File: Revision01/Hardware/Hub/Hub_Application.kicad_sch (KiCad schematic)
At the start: 81 parts, among them J10 IDC 6Pin Male Header, J11 IDC 6Pin Male Header, J12 IDC 6Pin Male Header, J13 IDC 6Pin Male Header, J14 IDC 6Pin Male Header, J15 IDC 6Pin Female Socket, J16 IDC 6Pin Male Header, J17 IDC 6Pin Female Socket, J18 IDC 6Pin Female Socket, J19 SMA-J-P-H-ST-EM1, J6 IDC 6Pin Male Header, J7 IDC 6Pin Male Header, J8 IDC 6Pin Male Header, J9 IDC 6Pin Male Header, Q1 PMOS, Q2 NMOS, Q3 PMOS, U3 MPU-6500, U4 Adafruit 3070

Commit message: . Moved / Renamed "Revision01" libraries to "Hub"
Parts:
- J10, J11, J12, J13, J14, J16, J6, J7, J8, J9: footprint Revision01:AdamTech_BHR-06-VUA -> Hub:AdamTech_BHR-06-VUA; symbol Revision01:IDC_6Pin_Male_Header -> Hub:IDC_6Pin_Male_Header
- J15, J17, J18: symbol Revision01:IDC_6Pin_Female_Socket -> Hub:IDC_6Pin_Female_Socket
- J19: symbol Revision01:ANT_SMA_Edge -> Hub:ANT_SMA_Edge
- R10: symbol Revision01:StrainGaugeFullBridge -> Hub:StrainGaugeFullBridge
- U3: footprint Revision01:MPU-6500_QFN40P300X300X95-25N -> Hub:MPU-6500_QFN40P300X300X95-25N; symbol Revision01:MPU-6500 -> Hub:MPU-6500
- U4: footprint Revision01:Adafruit3070 -> Hub:Adafruit3070; symbol Revision01:Adafruit3070 -> Hub:Adafruit3070
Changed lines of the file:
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@@
 	)
 	(symbol
-		(lib_id "Revision01:IDC_6Pin_Male_Header")
+		(lib_id "Hub:IDC_6Pin_Male_Header")
 		(at 66.04 195.58 0)
 		(unit 1)
@@
 			)
 		)
-		(property "Footprint" "Revision01:AdamTech_BHR-06-VUA"
+		(property "Footprint" "Hub:AdamTech_BHR-06-VUA"
 			(at 66.04 195.58 0)
 			(effects
@@
 	)
 	(symbol
-		(lib_id "Revision01:IDC_6Pin_Male_Header")
+		(lib_id "Hub:IDC_6Pin_Male_Header")
 		(at 148.59 118.11 0)
 		(unit 1)
@@
 			)
 		)
-		(property "Footprint" "Revision01:AdamTech_BHR-06-VUA"
+		(property "Footprint" "Hub:AdamTech_BHR-06-VUA"
 			(at 148.59 118.11 0)
 			(effects
@@
 	)
 	(symbol
-		(lib_id "Revision01:IDC_6Pin_Male_Header")
+		(lib_id "Hub:IDC_6Pin_Male_Header")
 		(at 148.59 80.01 0)
 		(unit 1)
@@
 			)
 		)
-		(property "Footprint" "Revision01:AdamTech_BHR-06-VUA"
+		(property "Footprint" "Hub:AdamTech_BHR-06-VUA"
 			(at 148.59 80.01 0)
 			(effects
@@
 	)
 	(symbol
-		(lib_id "Revision01:IDC_6Pin_Male_Header")
+		(lib_id "Hub:IDC_6Pin_Male_Header")
 		(at 148.59 105.41 0)
 		(unit 1)
@@
 			)
 		)
-		(property "Footprint" "Revision01:AdamTech_BHR-06-VUA"
+		(property "Footprint" "Hub:AdamTech_BHR-06-VUA"
 			(at 148.59 105.41 0)
 			(effects
@@
 	)
 	(symbol
-		(lib_id "Revision01:ANT_SMA_Edge")
+		(lib_id "Hub:ANT_SMA_Edge")
 		(at 349.25 203.2 0)
 		(unit 1)
@@
 	)
 	(symbol
-		(lib_id "Revision01:Adafruit3070")
+		(lib_id "Hub:Adafruit3070")
 		(at 285.75 179.07 0)
 		(unit 1)
@@
 			)
 		)
-		(property "Footprint" "Revision01:Adafruit3070"
+		(property "Footprint" "Hub:Adafruit3070"
 			(at 285.75 179.07 0)
 			(effects
@@
 	)
 	(symbol
-		(lib_id "Revision01:IDC_6Pin_Male_Header")
+		(lib_id "Hub:IDC_6Pin_Male_Header")
 		(at 148.59 168.91 0)
 		(unit 1)
@@
 			)
 		)
-		(property "Footprint" "Revision01:AdamTech_BHR-06-VUA"
+		(property "Footprint" "Hub:AdamTech_BHR-06-VUA"
 			(at 148.59 168.91 0)
 			(effects
@@
 	)
 	(symbol
-		(lib_id "Revision01:StrainGaugeFullBridge")
+		(lib_id "Hub:StrainGaugeFullBridge")
 		(at 149.86 53.34 0)
 		(unit 1)
@@
 	)
 	(symbol
-		(lib_id "Revision01:IDC_6Pin_Male_Header")
+		(lib_id "Hub:IDC_6Pin_Male_Header")
 		(at 101.6 195.58 0)
 		(unit 1)
@@
 			)
 		)
-		(property "Footprint" "Revision01:AdamTech_BHR-06-VUA"
+		(property "Footprint" "Hub:AdamTech_BHR-06-VUA"
 			(at 101.6 195.58 0)
 			(effects
@@
 	)
 	(symbol
-		(lib_id "Revision01:IDC_6Pin_Female_Socket")
+		(lib_id "Hub:IDC_6Pin_Female_Socket")
 		(at 83.82 195.58 0)
 		(mirror y)
@@
 	)
 	(symbol
-		(lib_id "Revision01:IDC_6Pin_Male_Header")
+		(lib_id "Hub:IDC_6Pin_Male_Header")
 		(at 148.59 143.51 0)
 		(unit 1)
@@
 			)
 		)
-		(property "Footprint" "Revision01:AdamTech_BHR-06-VUA"
+		(property "Footprint" "Hub:AdamTech_BHR-06-VUA"
 			(at 148.59 143.51 0)
 			(effects
@@
 	)
 	(symbol
-		(lib_id "Revision01:MPU-6500")
+		(lib_id "Hub:MPU-6500")
 		(at 321.31 110.49 0)
 		(unit 1)
@@
 			)
 		)
-		(property "Footprint" "Revision01:MPU-6500_QFN40P300X300X95-25N"
+		(property "Footprint" "Hub:MPU-6500_QFN40P300X300X95-25N"
 			(at 321.31 93.98 0)
 			(effects
@@
 	)
 	(symbol
-		(lib_id "Revision01:IDC_6Pin_Female_Socket")
+		(lib_id "Hub:IDC_6Pin_Female_Socket")
 		(at 120.65 195.58 0)
 		(mirror y)
@@
 	)
 	(symbol
-		(lib_id "Revision01:IDC_6Pin_Male_Header")
+		(lib_id "Hub:IDC_6Pin_Male_Header")
 		(at 148.59 92.71 0)
 		(unit 1)
@@
 			)
 		)
-		(property "Footprint" "Revision01:AdamTech_BHR-06-VUA"
+		(property "Footprint" "Hub:AdamTech_BHR-06-VUA"
 			(at 148.59 92.71 0)
 			(effects
@@
 	)
 	(symbol
-		(lib_id "Revision01:IDC_6Pin_Male_Header")
+		(lib_id "Hub:IDC_6Pin_Male_Header")
 		(at 148.59 156.21 0)
 		(unit 1)
@@
 			)
 		)
-		(property "Footprint" "Revision01:AdamTech_BHR-06-VUA"
+		(property "Footprint" "Hub:AdamTech_BHR-06-VUA"
 			(at 148.59 156.21 0)
 			(effects
@@
 	)
 	(symbol
-		(lib_id "Revision01:IDC_6Pin_Female_Socket")
+		(lib_id "Hub:IDC_6Pin_Female_Socket")
 		(at 133.35 195.58 0)
 		(unit 1)
@@
 	)
 	(symbol
-		(lib_id "Revision01:IDC_6Pin_Male_Header")
+		(lib_id "Hub:IDC_6Pin_Male_Header")
 		(at 148.59 130.81 0)
 		(unit 1)
@@
 			)
 		)
-		(property "Footprint" "Revision01:AdamTech_BHR-06-VUA"
+		(property "Footprint" "Hub:AdamTech_BHR-06-VUA"
 			(at 148.59 130.81 0)
 			(effects

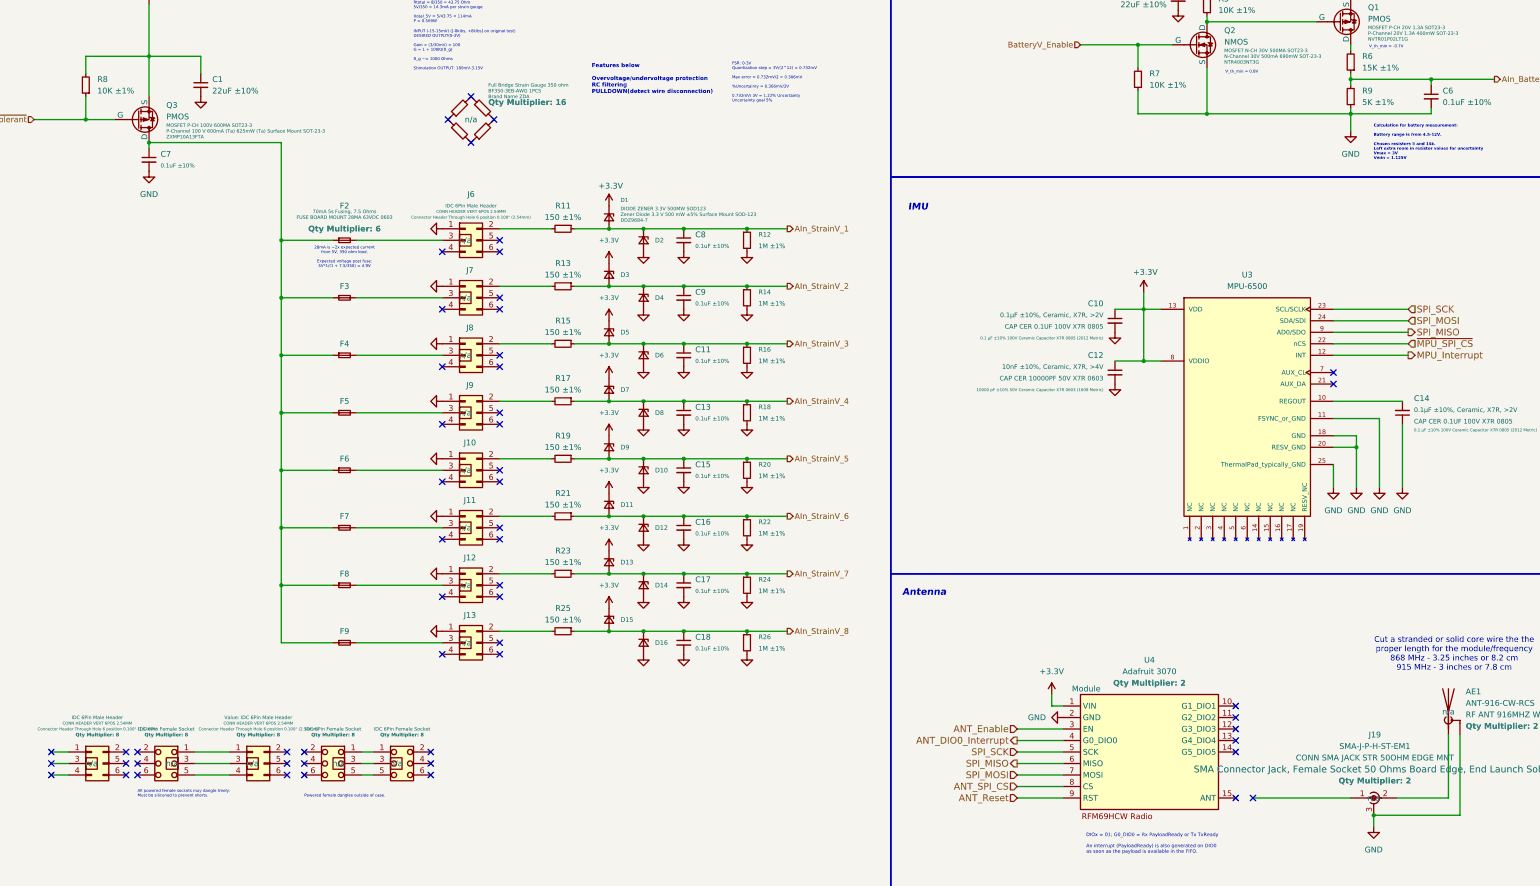
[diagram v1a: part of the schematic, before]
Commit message: . Split Hub symbol fields for Distributor Link/Part into DigiKey & AliExpress Link/Part in preparation for Mouser column.
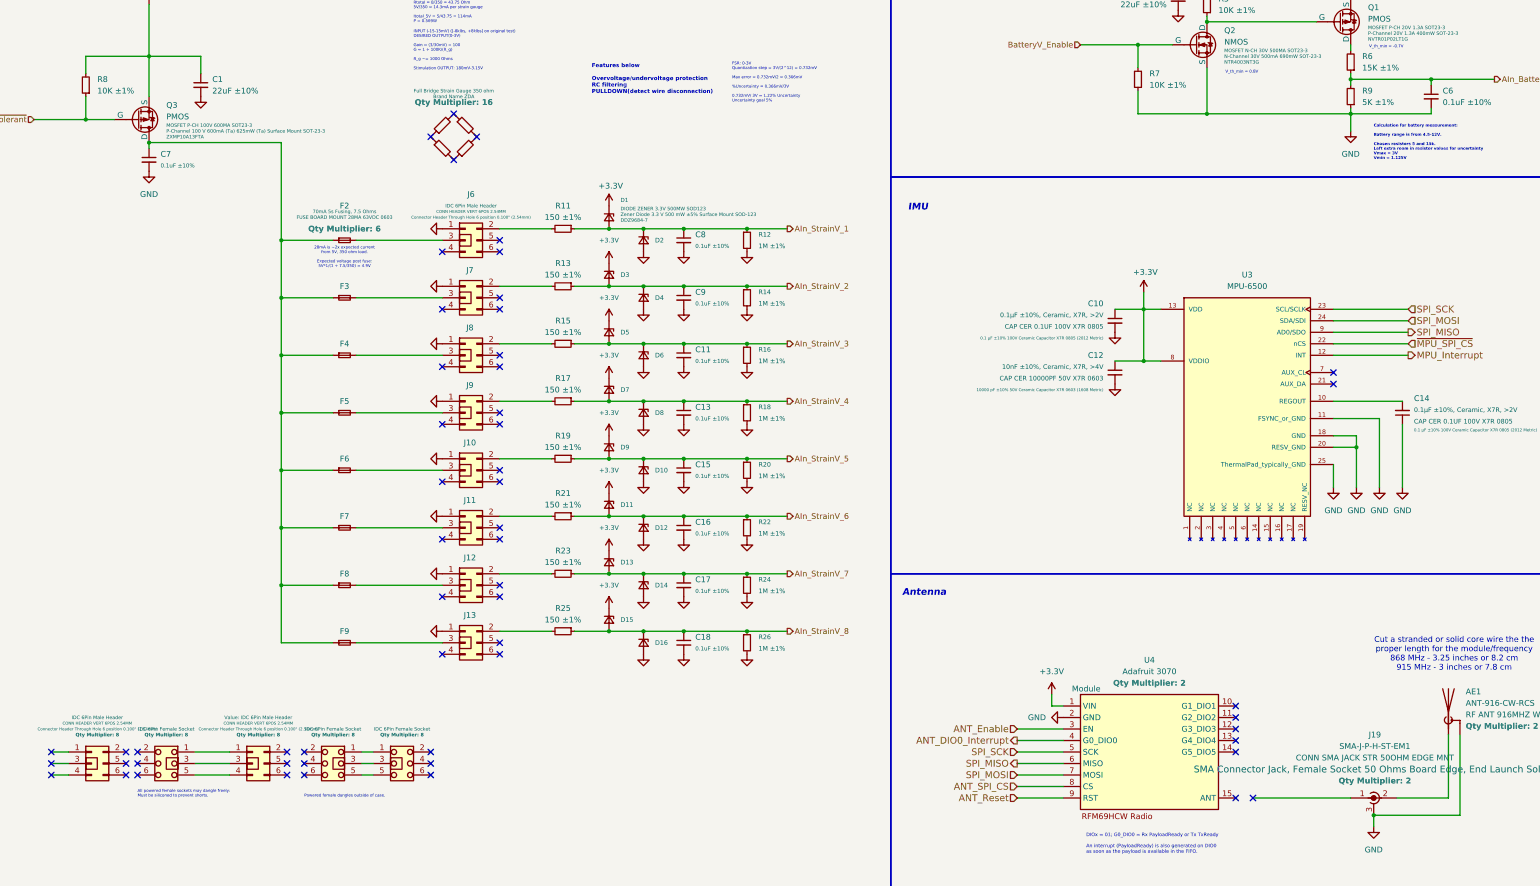
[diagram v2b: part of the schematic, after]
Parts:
- AE1: DigiKey Link (none) -> https://www.digikey.ca/en/products/detail/te-connectivity-l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; DigiKey Part Number (none) -> ANT-916-CW-RCS-ND; Distributor Link https://www.digikey.ca/en/products/detail/te-connectivity-l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 -> (none); Distributor Part Number ANT-916-CW-RCS-ND -> (none)
- C1, C19: DigiKey Link (none) -> https://www.digikey.ca/en/products/detail/samsung-electro-m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; DigiKey Part Number (none) -> 1276-3047-1-ND - Cut Tape (CT); Distributor Link https://www.digikey.ca/en/products/detail/samsung-electro-m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 -> (none); Distributor Part Number 1276-3047-1-ND - Cut Tape (CT) -> (none)
- C10, C11, C13, C14, C15, C16, C17, C18, C6, C7, C8, C9: DigiKey Link (none) -> https://www.digikey.ca/en/products/detail/samsung-electro-m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; DigiKey Part Number (none) -> 1276-6840-1-ND - Cut Tape (CT); Distributor Link https://www.digikey.ca/en/products/detail/samsung-electro-m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 -> (none); Distributor Part Number 1276-6840-1-ND - Cut Tape (CT) -> (none)
- C12: DigiKey Link (none) -> https://www.digikey.ca/en/products/detail/samsung-electro-m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; DigiKey Part Number (none) -> 1276-CL10B103KB8WPNDCT-ND - Cut Tape (CT); Distributor Link https://www.digikey.ca/en/products/detail/samsung-electro-m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 -> (none); Distributor Part Number 1276-CL10B103KB8WPNDCT-ND - Cut Tape (CT) -> (none)
- D1, D10, D11, D12, D13, D14, D15, D16, D2, D3, D4, D5, D6, D7, D8, D9: DigiKey Link (none) -> https://www.digikey.ca/en/products/detail/diodes-incorporat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; DigiKey Part Number (none) -> DDZ9684-7DITR-ND; Distributor Link https://www.digikey.ca/en/products/detail/diodes-incorporat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 -> (none); Distributor Part Number DDZ9684-7DITR-ND -> (none)
- F2, F3, F4, F5, F6, F7, F8, F9: DigiKey Link (none) -> https://www.digikey.ca/en/products/detail/kyocera-avx/F0603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; DigiKey Part Number (none) -> 478-13097-1-ND - Cut Tape (CT); Distributor Link https://www.digikey.ca/en/products/detail/kyocera-avx/F0603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 -> (none); Distributor Part Number 478-13097-1-ND - Cut Tape (CT) -> (none)
- J10, J11, J12, J13, J14, J16, J6, J7, J8, J9: DigiKey Link (none) -> https://www.digikey.ca/en/products/detail/adam-tech/BHR-06-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; DigiKey Part Number (none) -> 2057-BHR-06-VUA-ND; Distributor Link https://www.digikey.ca/en/products/detail/adam-tech/BHR-06-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 -> (none); Distributor Part Number 2057-BHR-06-VUA-ND -> (none)
- J15, J17, J18: DigiKey Link (none) -> https://www.digikey.ca/en/products/detail/adam-tech/FCS-06-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; DigiKey Part Number (none) -> 2057-FCS-06-SG-ND; Distributor Link https://www.digikey.ca/en/products/detail/adam-tech/FCS-06-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 -> (none); Distributor Part Number 2057-FCS-06-SG-ND -> (none)
- J19: DigiKey Link (none) -> https://www.digikey.ca/en/products/detail/samtec-inc/SMA-J-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; DigiKey Part Number (none) -> SAM8857-ND; Distributor Link https://www.digikey.ca/en/products/detail/samtec-inc/SMA-J-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 -> (none); Distributor Part Number SAM8857-ND -> (none)
- Q1: DigiKey Link (none) -> https://www.digikey.ca/en/products/detail/onsemi/NVTR01P02L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; DigiKey Part Number (none) -> NVTR01P02LT1GOSCT-ND; Distributor Link https://www.digikey.ca/en/products/detail/onsemi/NVTR01P02L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 -> (none); Distributor Part Number NVTR01P02LT1GOSCT-ND -> (none)
- Q2: DigiKey Link (none) -> https://www.digikey.ca/en/products/detail/onsemi/NTR4003NT3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; DigiKey Part Number (none) -> NTR4003NT3GOSCT-ND - Cut Tape (CT); Distributor Link https://www.digikey.ca/en/products/detail/onsemi/NTR4003NT3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 -> (none); Distributor Part Number NTR4003NT3GOSCT-ND - Cut Tape (CT) -> (none)
- Q3: DigiKey Link (none) -> https://www.digikey.ca/en/products/detail/diodes-incorporat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; DigiKey Part Number (none) -> ZXMP10A13FTR-ND; Distributor Link https://www.digikey.ca/en/products/detail/diodes-incorporat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 -> (none); Distributor Part Number ZXMP10A13FTR-ND -> (none)
- R10: AliExpress Link (none) -> https://www.aliexpress.com/item/1005006546478858.html; AliExpress Part Number (none) -> BF350-3EB-AWG 1PCS; DigiKey Link (none) -> https://www.aliexpress.com/item/1005006546478858.html; Distributor Link https://www.aliexpress.com/item/1005006546478858.html -> (none); Distributor Part Number BF350-3EB-AWG 1PCS -> (none)
- R11, R13, R15, R17, R19, R21, R23, R25: DigiKey Link (none) -> https://www.digikey.ca/en/products/detail/vishay-dale/CRCW0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; DigiKey Part Number (none) -> 541-150CTR-ND; Distributor Link https://www.digikey.ca/en/products/detail/vishay-dale/CRCW0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 -> (none); Distributor Part Number 541-150CTR-ND -> (none)
- R12, R14, R16, R18, R20, R22, R24, R26: DigiKey Link (none) -> https://www.digikey.ca/en/products/detail/vishay-dale/CRCW0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; DigiKey Part Number (none) -> 541-1.00MCCT-ND - Cut Tape (CT); Distributor Link https://www.digikey.ca/en/products/detail/vishay-dale/CRCW0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 -> (none); Distributor Part Number 541-1.00MCCT-ND - Cut Tape (CT) -> (none)
- R5, R7, R8: DigiKey Link (none) -> https://www.digikey.ca/en/products/detail/vishay-dale/CRCW0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; DigiKey Part Number (none) -> 541-10.0KCCT-ND - Cut Tape (CT); Distributor Link https://www.digikey.ca/en/products/detail/vishay-dale/CRCW0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 -> (none); Distributor Part Number 541-10.0KCCT-ND - Cut Tape (CT) -> (none)
- R6: DigiKey Link (none) -> https://www.digikey.ca/en/products/detail/vishay-dale/CRCW0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; DigiKey Part Number (none) -> 541-15.0KCCT-ND - Cut Tape (CT); Distributor Link https://www.digikey.ca/en/products/detail/vishay-dale/CRCW0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 -> (none); Distributor Part Number 541-15.0KCCT-ND - Cut Tape (CT) -> (none)
- R9: DigiKey Link (none) -> https://www.digikey.ca/en/products/detail/vishay-dale/CRCW0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; DigiKey Part Number (none) -> 541-CRCW08055K00FKTACT-ND - Cut Tape (CT); Distributor Link https://www.digikey.ca/en/products/detail/vishay-dale/CRCW0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 -> (none); Distributor Part Number 541-CRCW08055K00FKTACT-ND - Cut Tape (CT) -> (none)
- U3: DigiKey Link (none) -> https://www.digikey.ca/en/products/detail/tdk-invensense/MP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; DigiKey Part Number (none) -> 1428-1011-1-ND - Cut Tape (CT); Distributor Link https://www.digikey.ca/en/products/detail/tdk-invensense/MP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 -> (none); Distributor Part Number 1428-1011-1-ND - Cut Tape (CT) -> (none)
- U4: DigiKey Link (none) -> https://www.digikey.ca/en/products/detail/adafruit-industri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; DigiKey Part Number (none) -> 1528-1665-ND; Distributor Link https://www.digikey.ca/en/products/detail/adafruit-industri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 -> (none); Distributor Part Number 1528-1665-ND -> (none)
